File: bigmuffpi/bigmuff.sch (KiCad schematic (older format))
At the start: 62 parts, among them J1 PWR JACK, J4 OUTPUT, J5 INPUT, Q1 BC239, Q2 BC239, Q3 BC239, Q4 BC239, SW1 POWER

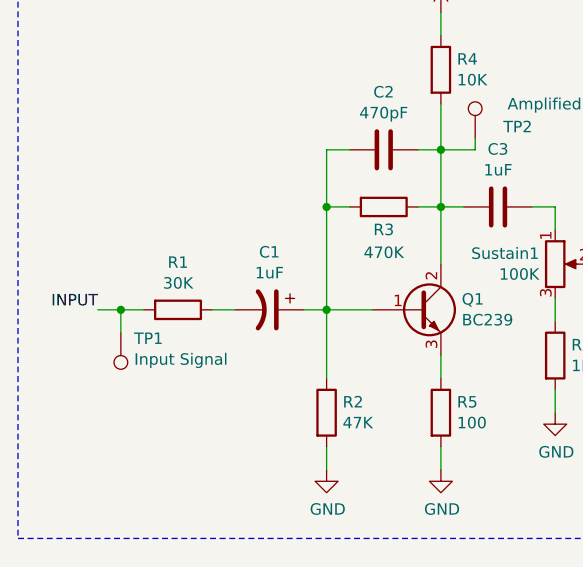
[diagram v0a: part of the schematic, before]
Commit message: fix: wrong input resistor
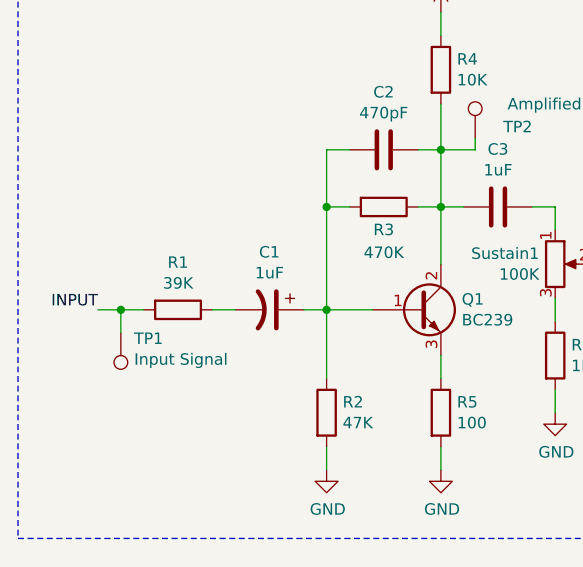
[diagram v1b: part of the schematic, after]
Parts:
- R1: value 30K -> 39K; Mfr. No CFR-12JB-52-30K -> CFR-12JR-52-39K; Mouser 603-CFR-12JB-52-30K -> 603-CFR-12JR-52-39K
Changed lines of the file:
@@
 P 1800 4000
 F 0 "R1" V 1593 4000 50  0000 C CNN
-F 1 "30K" V 1684 4000 50  0000 C CNN
+F 1 "39K" V 1684 4000 50  0000 C CNN
 F 2 "Resistor_THT:R_Axial_DIN0207_L6.3mm_D2.5mm_P10.16mm_Horizontal" V 1730 4000 50  0001 C CNN
 F 3 "https://cz.mouser.com/datasheet/2/447/yageo_yagos02873-1-1745585.pdf" H 1800 4000 50  0001 C CNN
-F 4 "CFR-12JB-52-30K" H 1800 4000 50  0001 C CNN "Mfr. No"
-F 5 "603-CFR-12JB-52-30K" H 1800 4000 50  0001 C CNN "Mouser"
+F 4 "CFR-12JR-52-39K" H 1800 4000 50  0001 C CNN "Mfr. No"
+F 5 "603-CFR-12JR-52-39K" H 1800 4000 50  0001 C CNN "Mouser"
 F 6 "Mouser" H 1800 4000 50  0001 C CNN "Supplier"
 	1    1800 4000

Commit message: fix: change resistor model
On the previous one min. order is 5000 pieces
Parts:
- R1, R17: Mfr. No CFR-12JR-52-39K -> CFR-12JB-52-39K; Mouser 603-CFR-12JR-52-39K -> 603-CFR-12JB-52-39K
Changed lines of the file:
@@
 F 2 "Resistor_THT:R_Axial_DIN0207_L6.3mm_D2.5mm_P10.16mm_Horizontal" V 1730 4000 50  0001 C CNN
 F 3 "https://cz.mouser.com/datasheet/2/447/yageo_yagos02873-1-1745585.pdf" H 1800 4000 50  0001 C CNN
-F 4 "CFR-12JR-52-39K" H 1800 4000 50  0001 C CNN "Mfr. No"
-F 5 "603-CFR-12JR-52-39K" H 1800 4000 50  0001 C CNN "Mouser"
+F 4 "CFR-12JB-52-39K" H 1800 4000 50  0001 C CNN "Mfr. No"
+F 5 "603-CFR-12JB-52-39K" H 1800 4000 50  0001 C CNN "Mouser"
 F 6 "Mouser" H 1800 4000 50  0001 C CNN "Supplier"
 	1    1800 4000
@@
 F 2 "Resistor_THT:R_Axial_DIN0207_L6.3mm_D2.5mm_P10.16mm_Horizontal" V 7880 3800 50  0001 C CNN
 F 3 "https://cz.mouser.com/datasheet/2/447/yageo_yagos02873-1-1745585.pdf" H 7950 3800 50  0001 C CNN
-F 4 "CFR-12JR-52-39K" H 7950 3800 50  0001 C CNN "Mfr. No"
-F 5 "603-CFR-12JR-52-39K" H 7950 3800 50  0001 C CNN "Mouser"
+F 4 "CFR-12JB-52-39K" H 7950 3800 50  0001 C CNN "Mfr. No"
+F 5 "603-CFR-12JB-52-39K" H 7950 3800 50  0001 C CNN "Mouser"
 F 6 "Mouser" H 7950 3800 50  0001 C CNN "Supplier"
 	1    7950 3800

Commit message: fix: wide footprint for transistors
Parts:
- Q1, Q2, Q3, Q4: footprint Package_TO_SOT_THT:TO-92L_Inline -> Package_TO_SOT_THT:TO-92L_Inline_Wide
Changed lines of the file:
@@
 F 0 "Q1" H 3041 4046 50  0000 L CNN
 F 1 "BC239" H 3041 3955 50  0000 L CNN
-F 2 "Package_TO_SOT_THT:TO-92L_Inline" H 3050 4100 50  0001 C CNN
+F 2 "Package_TO_SOT_THT:TO-92L_Inline_Wide" H 3050 4100 50  0001 C CNN
 F 3 "https://cz.mouser.com/datasheet/2/308/BC550-D-1802078.pdf" H 2850 4000 50  0001 C CNN
 F 4 "BC549CTA" H 2850 4000 50  0001 C CNN "Mfr. No"
@@
 F 0 "Q2" H 5341 3846 50  0000 L CNN
 F 1 "BC239" H 5341 3755 50  0000 L CNN
-F 2 "Package_TO_SOT_THT:TO-92L_Inline" H 5350 3900 50  0001 C CNN
+F 2 "Package_TO_SOT_THT:TO-92L_Inline_Wide" H 5350 3900 50  0001 C CNN
 F 3 "https://cz.mouser.com/datasheet/2/308/BC550-D-1802078.pdf" H 5150 3800 50  0001 C CNN
 F 4 "BC549CTA" H 5150 3800 50  0001 C CNN "Mfr. No"
@@
 F 0 "Q4" H 9541 3596 50  0000 L CNN
 F 1 "BC239" H 9541 3505 50  0000 L CNN
-F 2 "Package_TO_SOT_THT:TO-92L_Inline" H 9550 3650 50  0001 C CNN
+F 2 "Package_TO_SOT_THT:TO-92L_Inline_Wide" H 9550 3650 50  0001 C CNN
 F 3 "https://cz.mouser.com/datasheet/2/308/BC550-D-1802078.pdf" H 9350 3550 50  0001 C CNN
 F 4 "BC549CTA" H 9350 3550 50  0001 C CNN "Mfr. No"
@@
 F 0 "Q3" H 7191 3846 50  0000 L CNN
 F 1 "BC239" H 7191 3755 50  0000 L CNN
-F 2 "Package_TO_SOT_THT:TO-92L_Inline" H 7200 3900 50  0001 C CNN
+F 2 "Package_TO_SOT_THT:TO-92L_Inline_Wide" H 7200 3900 50  0001 C CNN
 F 3 "https://cz.mouser.com/datasheet/2/308/BC550-D-1802078.pdf" H 7000 3800 50  0001 C CNN
 F 4 "BC549CTA" H 7000 3800 50  0001 C CNN "Mfr. No"

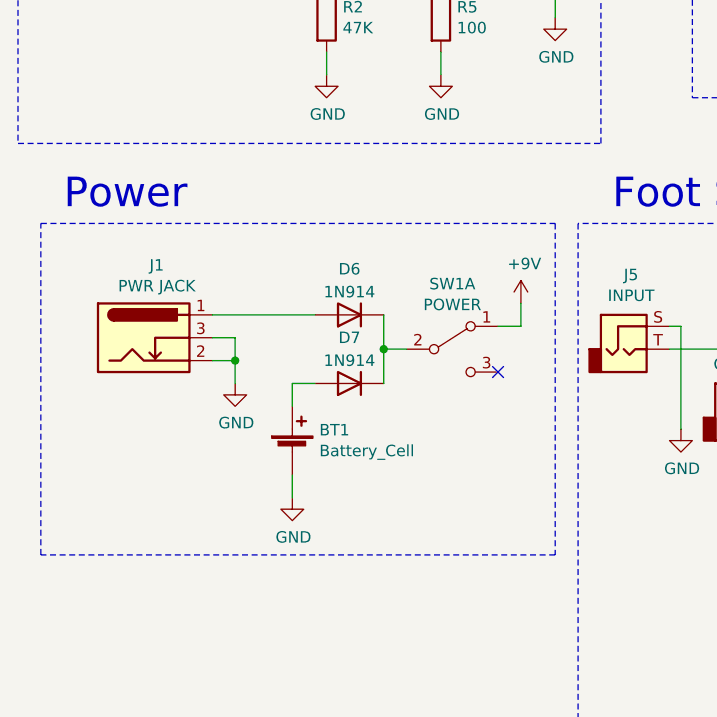
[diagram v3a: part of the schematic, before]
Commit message: add: reverse polarity protection based on PPTC
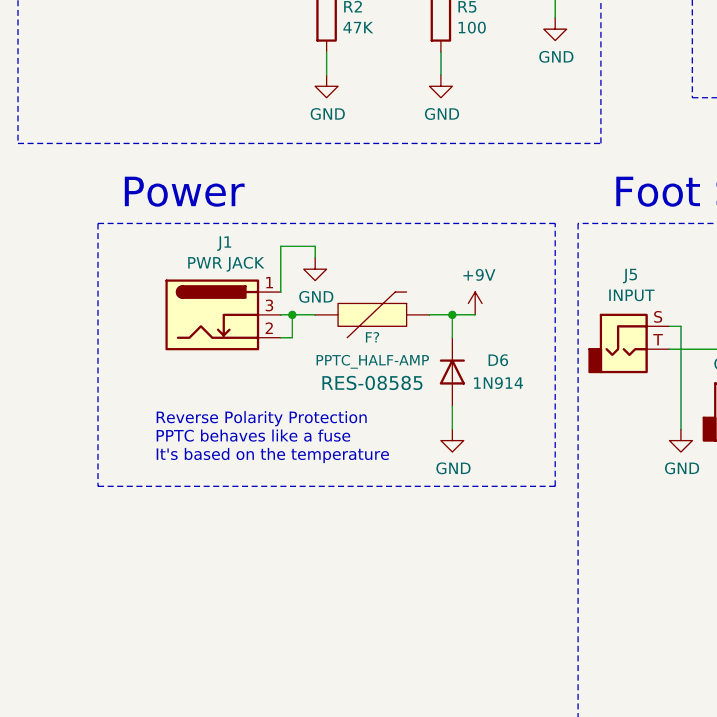
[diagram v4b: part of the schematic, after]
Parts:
- removed BT1: Battery_Cell, LED_THT:LED_D5.0mm, symbol Device:Battery_Cell
- removed D7: 1N914, Diode_THT:D_DO-35_SOD27_P7.62mm_Horizontal, symbol Device:D
- removed SW1: POWER, bigmuffpi:E-SWITCH-100SP3T2B4M6RE, symbol Switch:SW_DPDT_x2
- added F?: PPTC_HALF-AMP, 1206, symbol SparkFun-Fuses:PPTC_HALF-AMP
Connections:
- net +9V: now also D6.1 (K), F?.2
- net GND: now also D6.2 (A), J1.1; no longer J1.2, J1.3
- new net: F?.1, J1.2, J1.3
- no-connect marks 2 -> 1
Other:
- note added: "Reverse Polarity Protection\nPPTC behaves like a fuse\nIt's based on the temperature"
- moved on the sheet: D6, J1
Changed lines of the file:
@@
 Output Booster
-$Comp
-L power:GND #PWR020
-U 1 1 5EDC192C
-P 2300 6550
-F 0 "#PWR020" H 2300 6300 50  0001 C CNN
-F 1 "GND" H 2305 6377 50  0000 C CNN
-F 2 "" H 2300 6550 50  0001 C CNN
-F 3 "" H 2300 6550 50  0001 C CNN
-	1    2300 6550
-	1    0    0    -1
-$EndComp
 $Comp
 L power:+9V #PWR019
 U 1 1 5EDC6BC5
-P 3300 5700
-F 0 "#PWR019" H 3300 5550 50  0001 C CNN
-F 1 "+9V" H 3315 5873 50  0000 C CNN
-F 2 "" H 3300 5700 50  0001 C CNN
-F 3 "" H 3300 5700 50  0001 C CNN
-	1    3300 5700
-	1    0    0    -1
-$EndComp
-Wire Wire Line
-	2300 6550 2300 6450
+P 3100 5750
+F 0 "#PWR019" H 3100 5600 50  0001 C CNN
+F 1 "+9V" H 3115 5923 50  0000 C CNN
+F 2 "" H 3100 5750 50  0001 C CNN
+F 3 "" H 3100 5750 50  0001 C CNN
+	1    3100 5750
+	1    0    0    -1
+$EndComp
 Text Label 1450 4000 2    50   ~ 0
 INPUT
@@
 Text Notes 3700 5300 0    129  ~ 0
 Foot Switch\n
-Text Notes 1300 5300 0    129  ~ 0
+Text Notes 1550 5300 0    129  ~ 0
 Power
 $Comp
@@
 	1    0    0    -1
 $EndComp
-$Comp
-L Switch:SW_DPDT_x2 SW1
-U 1 1 5EF7480B
-P 3000 5900
-F 0 "SW1" H 3000 6185 50  0000 C CNN
-F 1 "POWER" H 3000 6094 50  0000 C CNN
-F 2 "bigmuffpi:E-SWITCH-100SP3T2B4M6RE" H 3000 5900 50  0001 C CNN
-F 3 "https://cz.mouser.com/datasheet/2/140/100-1079940.pdf" H 3000 5900 50  0001 C CNN
-F 4 "100SP3T2B4M6RE" H 3000 5900 50  0001 C CNN "Mfr. No"
-F 5 "612-100-A1111" H 3000 5900 50  0001 C CNN "Mouser"
-F 6 "LCSC" H 3000 5900 50  0001 C CNN "Supplier"
-F 7 "C273357" H 3000 5900 50  0001 C CNN "LCSC"
-	1    3000 5900
-	1    0    0    -1
-$EndComp
-Wire Wire Line
-	3200 5800 3300 5800
-Wire Wire Line
-	3300 5800 3300 5700
-NoConn ~ 3200 6000
 $Comp
 L SparkFun-Switches:3PDT-foot-switch S1
@@
 L Connector:Barrel_Jack_Switch J1
 U 1 1 5F0D54E6
-P 1650 5850
-F 0 "J1" H 1707 6167 50  0000 C CNN
-F 1 "PWR JACK" H 1707 6076 50  0000 C CNN
-F 2 "Connector_PinHeader_2.54mm:PinHeader_1x03_P2.54mm_Vertical" H 1700 5810 50  0001 C CNN
-F 3 "https://www.aliexpress.com/wholesale?catId=0&SearchText=panel+mount+barrel+jack" H 1700 5810 50  0001 C CNN
-F 4 "" H 1650 5850 50  0001 C CNN "LCSC"
-F 5 "" H 1650 5850 50  0001 C CNN "Mfr. No"
-F 6 "Aliexpress" H 1650 5850 50  0001 C CNN "Supplier"
-	1    1650 5850
+P 1950 5750
+F 0 "J1" H 2007 6067 50  0000 C CNN
+F 1 "PWR JACK" H 2007 5976 50  0000 C CNN
+F 2 "Connector_PinHeader_2.54mm:PinHeader_1x03_P2.54mm_Vertical" H 2000 5710 50  0001 C CNN
+F 3 "https://www.aliexpress.com/wholesale?catId=0&SearchText=panel+mount+barrel+jack" H 2000 5710 50  0001 C CNN
+F 4 "" H 1950 5750 50  0001 C CNN "LCSC"
+F 5 "" H 1950 5750 50  0001 C CNN "Mfr. No"
+F 6 "Aliexpress" H 1950 5750 50  0001 C CNN "Supplier"
+	1    1950 5750
 	1    0    0    -1
 $EndComp
@@
 L Device:D D6
 U 1 1 5F0DF5EC
-P 2550 5750
-F 0 "D6" H 2550 5550 50  0000 C CNN
-F 1 "1N914" H 2550 5650 50  0000 C CNN
-F 2 "Diode_THT:D_DO-35_SOD27_P7.62mm_Horizontal" H 2550 5750 50  0001 C CNN
-F 3 "https://cz.mouser.com/datasheet/2/308/1N914-D-1801484.pdf" H 2550 5750 50  0001 C CNN
-F 4 "C125665" H 2550 5750 50  0001 C CNN "LCSC"
-F 5 "1N914" H 2550 5750 50  0001 C CNN "Mfr. No"
-F 6 "512-1N914" H 2550 5750 50  0001 C CNN "Mouser"
-F 7 "Mouser" H 2550 5750 50  0001 C CNN "Supplier"
-	1    2550 5750
-	-1   0    0    1
-$EndComp
-$Comp
-L Device:D D7
-U 1 1 5F0E34F6
-P 2550 6050
-F 0 "D7" H 2550 5850 50  0000 C CNN
-F 1 "1N914" H 2550 5950 50  0000 C CNN
-F 2 "Diode_THT:D_DO-35_SOD27_P7.62mm_Horizontal" H 2550 6050 50  0001 C CNN
-F 3 "https://cz.mouser.com/datasheet/2/308/1N914-D-1801484.pdf" H 2550 6050 50  0001 C CNN
-F 4 "C125665" H 2550 6050 50  0001 C CNN "LCSC"
-F 5 "1N914" H 2550 6050 50  0001 C CNN "Mfr. No"
-F 6 "512-1N914" H 2550 6050 50  0001 C CNN "Mouser"
-F 7 "Mouser" H 2550 6050 50  0001 C CNN "Supplier"
-	1    2550 6050
-	-1   0    0    1
+P 3000 6000
+F 0 "D6" V 2950 6200 50  0000 C CNN
+F 1 "1N914" V 3050 6200 50  0000 C CNN
+F 2 "Diode_THT:D_DO-35_SOD27_P7.62mm_Horizontal" H 3000 6000 50  0001 C CNN
+F 3 "https://cz.mouser.com/datasheet/2/308/1N914-D-1801484.pdf" H 3000 6000 50  0001 C CNN
+F 4 "C125665" H 3000 6000 50  0001 C CNN "LCSC"
+F 5 "1N914" H 3000 6000 50  0001 C CNN "Mfr. No"
+F 6 "512-1N914" H 3000 6000 50  0001 C CNN "Mouser"
+F 7 "Mouser" H 3000 6000 50  0001 C CNN "Supplier"
+	1    3000 6000
+	0    1    1    0
 $EndComp
 $Comp
 L power:GND #PWR023
 U 1 1 5F12432A
-P 2050 6050
-F 0 "#PWR023" H 2050 5800 50  0001 C CNN
-F 1 "GND" H 2055 5877 50  0000 C CNN
-F 2 "" H 2050 6050 50  0001 C CNN
-F 3 "" H 2050 6050 50  0001 C CNN
-	1    2050 6050
-	1    0    0    -1
-$EndComp
-Wire Wire Line
-	1950 5950 2050 5950
-Wire Wire Line
-	2050 5950 2050 6050
-Wire Wire Line
-	1950 5850 2050 5850
-Wire Wire Line
-	2050 5850 2050 5950
-Connection ~ 2050 5950
-$Comp
-L Device:Battery_Cell BT1
-U 1 1 5F14DC7A
-P 2300 6350
-F 0 "BT1" H 2418 6446 50  0000 L CNN
-F 1 "Battery_Cell" H 2418 6355 50  0000 L CNN
-F 2 "LED_THT:LED_D5.0mm" V 2300 6410 50  0001 C CNN
-F 3 "https://cz.mouser.com/datasheet/2/215/9-745395.pdf" V 2300 6410 50  0001 C CNN
-F 4 "79 " H 2300 6350 50  0001 C CNN "Mfr. No"
-F 5 "534-079 " H 2300 6350 50  0001 C CNN "Mouser"
-F 6 "Mouser" H 2300 6350 50  0001 C CNN "Supplier"
-	1    2300 6350
-	1    0    0    -1
-$EndComp
-Wire Wire Line
-	2300 6150 2300 6050
-Wire Wire Line
-	2300 6050 2400 6050
-Wire Wire Line
-	1950 5750 2400 5750
-Wire Wire Line
-	2700 5750 2700 5900
-Wire Wire Line
-	2700 5900 2800 5900
-Connection ~ 2700 5900
-Wire Wire Line
-	2700 5900 2700 6050
+P 2400 5500
+F 0 "#PWR023" H 2400 5250 50  0001 C CNN
+F 1 "GND" H 2405 5327 50  0000 C CNN
+F 2 "" H 2400 5500 50  0001 C CNN
+F 3 "" H 2400 5500 50  0001 C CNN
+	1    2400 5500
+	1    0    0    -1
+$EndComp
 $Comp
 L Connector:TestPoint TP1
@@
 Wire Wire Line
 	3950 5900 4650 5900
-Wire Notes Line
-	3450 5350 3450 6800
-Wire Notes Line
-	1200 5350 3450 5350
-Wire Notes Line
-	3450 6800 1200 6800
-Wire Notes Line
-	1200 6800 1200 5350
 Wire Wire Line
 	4600 6450 4600 6500
@@
 Wire Notes Line
 	6200 5350 6200 7650
+Wire Wire Line
+	2250 5750 2300 5750
+Wire Wire Line
+	2250 5850 2300 5850
+Wire Wire Line
+	2300 5850 2300 5750
+Wire Wire Line
+	2250 5650 2250 5450
+$Comp
+L SparkFun-Fuses:PPTC_HALF-AMP F?
+U 1 1 5F449675
+P 2600 5750
+F 0 "F?" H 2650 5650 45  0000 C CNN
+F 1 "PPTC_HALF-AMP" H 2650 5550 45  0000 C CNN
+F 2 "1206" H 2600 5950 20  0001 C CNN
+F 3 "" H 2600 5750 50  0001 C CNN
+F 4 "RES-08585" H 2650 5450 60  0000 C CNN "Field4"
+	1    2600 5750
+	1    0    0    -1
+$EndComp
+$Comp
+L power:GND #PWR?
+U 1 1 5F44D824
+P 3000 6250
+F 0 "#PWR?" H 3000 6000 50  0001 C CNN
+F 1 "GND" H 3005 6077 50  0000 C CNN
+F 2 "" H 3000 6250 50  0001 C CNN
+F 3 "" H 3000 6250 50  0001 C CNN
+	1    3000 6250
+	1    0    0    -1
+$EndComp
+Wire Wire Line
+	3000 6250 3000 6150
+Wire Wire Line
+	2900 5750 3000 5750
+Wire Wire Line
+	2400 5750 2300 5750
+Connection ~ 2300 5750
+Wire Wire Line
+	3000 5850 3000 5750
+Connection ~ 3000 5750
+Wire Wire Line
+	3000 5750 3100 5750
+Wire Wire Line
+	2250 5450 2400 5450
+Wire Wire Line
+	2400 5450 2400 5500
+Text Notes 1700 6400 0    50   ~ 0
+Reverse Polarity Protection\nPPTC behaves like a fuse\nIt's based on the temperature
+Wire Notes Line
+	1450 5350 1450 6500
+Wire Notes Line
+	1450 6500 3450 6500
+Wire Notes Line
+	3450 6500 3450 5350
+Wire Notes Line
+	1450 5350 3450 5350
 $EndSCHEMATC
